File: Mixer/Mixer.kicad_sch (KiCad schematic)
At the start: 39 parts, among them J1 EURO_PWR_2x5, J2 INPUT_1, J3 INPUT_2, J4 INPUT_3, J5 INPUT_4, J6 OUTPUT, U1 TL082

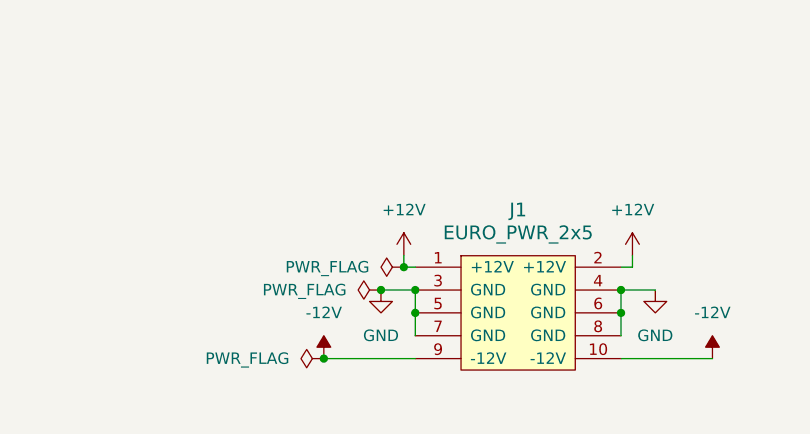
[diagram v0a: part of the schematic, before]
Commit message: Fix footprint for europower connector, add clearance for shrouded connector
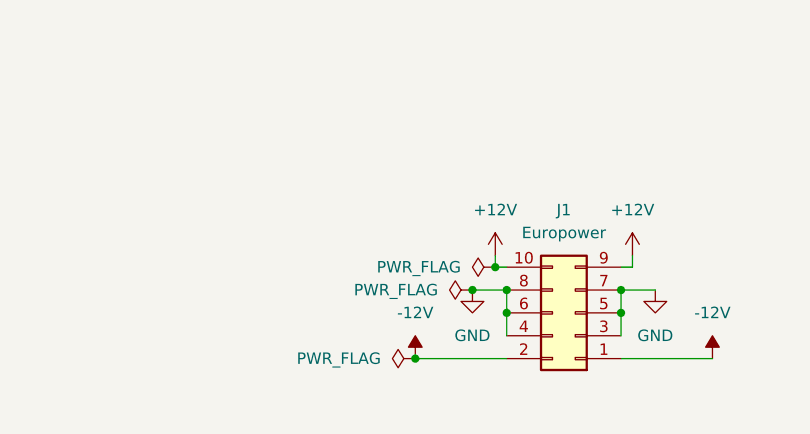
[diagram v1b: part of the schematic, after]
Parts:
- removed J1: EURO_PWR_2x5, Connector_PinHeader_2.54mm:PinHeader_2x05_P2.54mm_Vertical, symbol eurocad:EURO_PWR_2x5
- added J1: Europower, Connector_PinHeader_2.54mm:PinHeader_2x05_P2.54mm_Vertical, symbol Connector_Generic:Conn_02x05_Odd_Even
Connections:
- net +12V: now also J1.10 (Pin_10), J1.9 (Pin_9)
- net -12V: now also J1.1 (Pin_1), J1.2 (Pin_2)
- net GND: now also J1.3 (Pin_3), J1.4 (Pin_4), J1.5 (Pin_5), J1.6 (Pin_6), J1.7 (Pin_7), J1.8 (Pin_8)
